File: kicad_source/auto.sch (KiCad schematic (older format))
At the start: 24 parts, among them U14 NE555, U15 74xx175, U16 74xx00, U17 74xx175, U18 74xx32, U3 74xx08

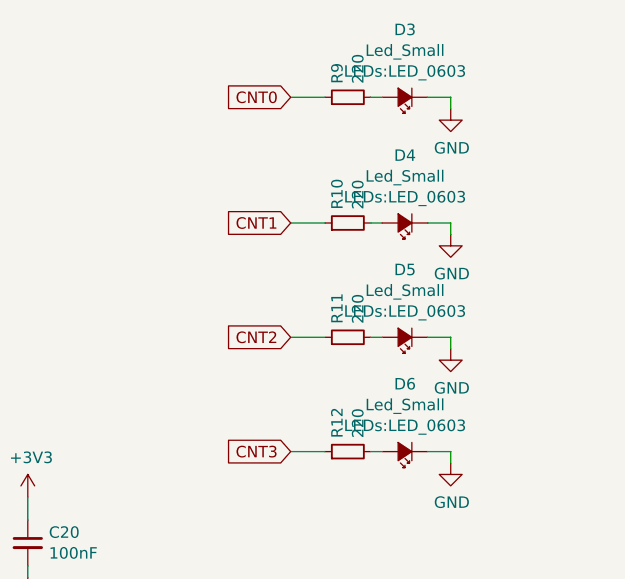
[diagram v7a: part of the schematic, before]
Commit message: added led digikey order numbers
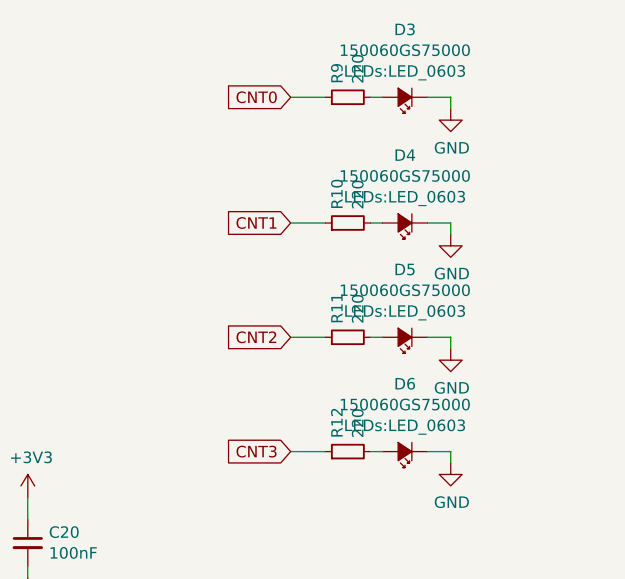
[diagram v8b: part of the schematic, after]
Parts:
- D3, D4, D5, D6: value Led_Small -> 150060GS75000
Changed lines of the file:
@@
 $EndDescr
-$Comp
-L IC_logic:NE555 U?
-U 1 1 5EDEF6C9
-P 3200 2150
-AR Path="/5EDEF6C9" Ref="U?"  Part="1"
-AR Path="/5EDDA6D0/5EDEF6C9" Ref="U14"  Part="1"
-F 0 "U14" H 3200 2675 50  0000 C CNN
-F 1 "NE555" H 3200 2584 50  0000 C CNN
-F 2 "SOIC:SOIC-8_3.9x4.9mm_Pitch1.27mm" H 3200 2150 50  0001 C CNN
-F 3 "" H 3200 2150 50  0001 C CNN
-	1    3200 2150
-	1    0    0    -1
-$EndComp
 $Comp
 L power-supply:+3V3 #PWR?
@@
 Text Label 4150 2250 0    50   ~ 0
 CLK_10Hz
-$Comp
-L IC_logic:74xx175 U?
-U 1 1 5EDF7AF9
-P 7300 4300
-AR Path="/5EDF7AF9" Ref="U?"  Part="1"
-AR Path="/5EDDA6D0/5EDF7AF9" Ref="U17"  Part="1"
-F 0 "U17" H 7300 4975 50  0000 C CNN
-F 1 "74xx175" H 7300 4884 50  0000 C CNN
-F 2 "SOIC:SOIC-16_3.9x9.9mm_Pitch1.27mm" H 7300 4300 50  0001 C CNN
-F 3 "" H 7300 4300 50  0001 C CNN
-	1    7300 4300
-	1    0    0    -1
-$EndComp
 Text GLabel 2550 3900 0    50   Input ~ 0
 AUTO
@@
 Wire Wire Line
 	7650 4550 8350 4550
-$Comp
-L IC_logic:74xx175 U?
-U 1 1 5EE42B61
-P 3650 5500
-AR Path="/5EE42B61" Ref="U?"  Part="1"
-AR Path="/5EDDA6D0/5EE42B61" Ref="U15"  Part="1"
-F 0 "U15" H 3650 6175 50  0000 C CNN
-F 1 "74xx175" H 3650 6084 50  0000 C CNN
-F 2 "SOIC:SOIC-16_3.9x9.9mm_Pitch1.27mm" H 3650 5500 50  0001 C CNN
-F 3 "" H 3650 5500 50  0001 C CNN
-	1    3650 5500
-	1    0    0    -1
-$EndComp
-$Comp
-L IC_logic:74xx00 U?
-U 1 1 5EE54782
-P 5050 4700
-AR Path="/5EE54782" Ref="U?"  Part="1"
-AR Path="/5EDDA6D0/5EE54782" Ref="U16"  Part="1"
-F 0 "U16" H 5050 5465 50  0000 C CNN
-F 1 "74xx00" H 5050 5374 50  0000 C CNN
-F 2 "SOIC:SOIC-14_3.9x8.7mm_Pitch1.27mm" H 5050 4700 50  0001 C CNN
-F 3 "" H 5050 4700 50  0001 C CNN
-	1    5050 4700
-	1    0    0    -1
-$EndComp
 Wire Wire Line
 	4750 4000 4600 4000
@@
 Wire Wire Line
 	9650 5900 9400 5900
-$Comp
-L IC_logic:74xx08 U3
-U 1 1 5EE4F2FA
-P 9750 5700
-F 0 "U3" H 9950 6387 60  0000 C CNN
-F 1 "74xx08" H 9950 6281 60  0000 C CNN
-F 2 "SOIC:SOIC-14_3.9x8.7mm_Pitch1.27mm" H 10050 5550 60  0001 C CNN
-F 3 "" H 9750 5700 60  0000 C CNN
-	1    9750 5700
-	1    0    0    -1
-$EndComp
-$Comp
-L IC_logic:74xx32 U18
-U 1 1 5EE50272
-P 9900 4850
-F 0 "U18" H 9950 6115 50  0000 C CNN
-F 1 "74xx32" H 9950 6024 50  0000 C CNN
-F 2 "SOIC:SOIC-14_3.9x8.7mm_Pitch1.27mm" H 9900 4850 50  0001 C CNN
-F 3 "" H 9900 4850 50  0001 C CNN
-	1    9900 4850
-	1    0    0    -1
-$EndComp
 Wire Wire Line
 	9650 6200 9500 6200
@@
 	0    -1   -1   0
 $EndComp
-$Comp
-L devices:Led_Small D?
-U 1 1 5EF5564B
-P 9950 1200
-AR Path="/5EF5564B" Ref="D?"  Part="1"
-AR Path="/5EDDA6D0/5EF5564B" Ref="D3"  Part="1"
-F 0 "D3" H 9950 905 50  0000 C CNN
-F 1 "Led_Small" H 9950 996 50  0000 C CNN
-F 2 "LEDs:LED_0603" H 9950 1087 50  0000 C CNN
-F 3 "" V 9950 1200 50  0000 C CNN
-	1    9950 1200
-	-1   0    0    1
-$EndComp
 Wire Wire Line
 	9850 1200 9800 1200
@@
 	0    -1   -1   0
 $EndComp
-$Comp
-L devices:Led_Small D?
-U 1 1 5EF6B35A
-P 9950 1750
-AR Path="/5EF6B35A" Ref="D?"  Part="1"
-AR Path="/5EDDA6D0/5EF6B35A" Ref="D4"  Part="1"
-F 0 "D4" H 9950 1455 50  0000 C CNN
-F 1 "Led_Small" H 9950 1546 50  0000 C CNN
-F 2 "LEDs:LED_0603" H 9950 1637 50  0000 C CNN
-F 3 "" V 9950 1750 50  0000 C CNN
-	1    9950 1750
-	-1   0    0    1
-$EndComp
 Wire Wire Line
 	9850 1750 9800 1750
@@
 	0    -1   -1   0
 $EndComp
-$Comp
-L devices:Led_Small D?
-U 1 1 5EF72578
-P 9950 2250
-AR Path="/5EF72578" Ref="D?"  Part="1"
-AR Path="/5EDDA6D0/5EF72578" Ref="D5"  Part="1"
-F 0 "D5" H 9950 1955 50  0000 C CNN
-F 1 "Led_Small" H 9950 2046 50  0000 C CNN
-F 2 "LEDs:LED_0603" H 9950 2137 50  0000 C CNN
-F 3 "" V 9950 2250 50  0000 C CNN
-	1    9950 2250
-	-1   0    0    1
-$EndComp
 Wire Wire Line
 	9850 2250 9800 2250
@@
 AR Path="/5EDDA6D0/5EF795BA" Ref="D6"  Part="1"
 F 0 "D6" H 9950 2455 50  0000 C CNN
-F 1 "Led_Small" H 9950 2546 50  0000 C CNN
+F 1 "150060GS75000" H 9950 2546 50  0000 C CNN
 F 2 "LEDs:LED_0603" H 9950 2637 50  0000 C CNN
 F 3 "" V 9950 2750 50  0000 C CNN
@@
 Text GLabel 9450 2750 0    50   Input ~ 0
 CNT3
+$Comp
+L IC_logic:74xx08 U3
+U 1 1 5EE4F2FA
+P 9750 5700
+F 0 "U3" H 9950 6387 60  0000 C CNN
+F 1 "74xx08" H 9950 6281 60  0000 C CNN
+F 2 "SOIC:SOIC-14_3.9x8.7mm_Pitch1.27mm" H 10050 5550 60  0001 C CNN
+F 3 "" H 9750 5700 60  0000 C CNN
+	1    9750 5700
+	1    0    0    -1
+$EndComp
+$Comp
+L IC_logic:74xx32 U18
+U 1 1 5EE50272
+P 9900 4850
+F 0 "U18" H 9950 6115 50  0000 C CNN
+F 1 "74xx32" H 9950 6024 50  0000 C CNN
+F 2 "SOIC:SOIC-14_3.9x8.7mm_Pitch1.27mm" H 9900 4850 50  0001 C CNN
+F 3 "" H 9900 4850 50  0001 C CNN
+	1    9900 4850
+	1    0    0    -1
+$EndComp
+$Comp
+L IC_logic:74xx175 U?
+U 1 1 5EE42B61
+P 3650 5500
+AR Path="/5EE42B61" Ref="U?"  Part="1"
+AR Path="/5EDDA6D0/5EE42B61" Ref="U15"  Part="1"
+F 0 "U15" H 3650 6175 50  0000 C CNN
+F 1 "74xx175" H 3650 6084 50  0000 C CNN
+F 2 "SOIC:SOIC-16_3.9x9.9mm_Pitch1.27mm" H 3650 5500 50  0001 C CNN
+F 3 "" H 3650 5500 50  0001 C CNN
+	1    3650 5500
+	1    0    0    -1
+$EndComp
+$Comp
+L IC_logic:74xx175 U?
+U 1 1 5EDF7AF9
+P 7300 4300
+AR Path="/5EDF7AF9" Ref="U?"  Part="1"
+AR Path="/5EDDA6D0/5EDF7AF9" Ref="U17"  Part="1"
+F 0 "U17" H 7300 4975 50  0000 C CNN
+F 1 "74xx175" H 7300 4884 50  0000 C CNN
+F 2 "SOIC:SOIC-16_3.9x9.9mm_Pitch1.27mm" H 7300 4300 50  0001 C CNN
+F 3 "" H 7300 4300 50  0001 C CNN
+	1    7300 4300
+	1    0    0    -1
+$EndComp
+$Comp
+L IC_logic:74xx00 U?
+U 1 1 5EE54782
+P 5050 4700
+AR Path="/5EE54782" Ref="U?"  Part="1"
+AR Path="/5EDDA6D0/5EE54782" Ref="U16"  Part="1"
+F 0 "U16" H 5050 5465 50  0000 C CNN
+F 1 "74xx00" H 5050 5374 50  0000 C CNN
+F 2 "SOIC:SOIC-14_3.9x8.7mm_Pitch1.27mm" H 5050 4700 50  0001 C CNN
+F 3 "" H 5050 4700 50  0001 C CNN
+	1    5050 4700
+	1    0    0    -1
+$EndComp
+$Comp
+L IC_logic:NE555 U?
+U 1 1 5EDEF6C9
+P 3200 2150
+AR Path="/5EDEF6C9" Ref="U?"  Part="1"
+AR Path="/5EDDA6D0/5EDEF6C9" Ref="U14"  Part="1"
+F 0 "U14" H 3200 2675 50  0000 C CNN
+F 1 "NE555" H 3200 2584 50  0000 C CNN
+F 2 "SOIC:SOIC-8_3.9x4.9mm_Pitch1.27mm" H 3200 2150 50  0001 C CNN
+F 3 "" H 3200 2150 50  0001 C CNN
+	1    3200 2150
+	1    0    0    -1
+$EndComp
+$Comp
+L devices:Led_Small D?
+U 1 1 5EF72578
+P 9950 2250
+AR Path="/5EF72578" Ref="D?"  Part="1"
+AR Path="/5EDDA6D0/5EF72578" Ref="D5"  Part="1"
+F 0 "D5" H 9950 1955 50  0000 C CNN
+F 1 "150060GS75000" H 9950 2046 50  0000 C CNN
+F 2 "LEDs:LED_0603" H 9950 2137 50  0000 C CNN
+F 3 "" V 9950 2250 50  0000 C CNN
+	1    9950 2250
+	-1   0    0    1
+$EndComp
+$Comp
+L devices:Led_Small D?
+U 1 1 5EF6B35A
+P 9950 1750
+AR Path="/5EF6B35A" Ref="D?"  Part="1"
+AR Path="/5EDDA6D0/5EF6B35A" Ref="D4"  Part="1"
+F 0 "D4" H 9950 1455 50  0000 C CNN
+F 1 "150060GS75000" H 9950 1546 50  0000 C CNN
+F 2 "LEDs:LED_0603" H 9950 1637 50  0000 C CNN
+F 3 "" V 9950 1750 50  0000 C CNN
+	1    9950 1750
+	-1   0    0    1
+$EndComp
+$Comp
+L devices:Led_Small D?
+U 1 1 5EF5564B
+P 9950 1200
+AR Path="/5EF5564B" Ref="D?"  Part="1"
+AR Path="/5EDDA6D0/5EF5564B" Ref="D3"  Part="1"
+F 0 "D3" H 9950 905 50  0000 C CNN
+F 1 "150060GS75000" H 9950 996 50  0000 C CNN
+F 2 "LEDs:LED_0603" H 9950 1087 50  0000 C CNN
+F 3 "" V 9950 1200 50  0000 C CNN
+	1    9950 1200
+	-1   0    0    1
+$EndComp
 $EndSCHEMATC
